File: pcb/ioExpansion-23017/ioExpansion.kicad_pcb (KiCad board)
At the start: 2 copper layers, 16 parts, among them J1 GS3, J2 GS3, J3 GS3, U1 MCP23017, U2 Header2

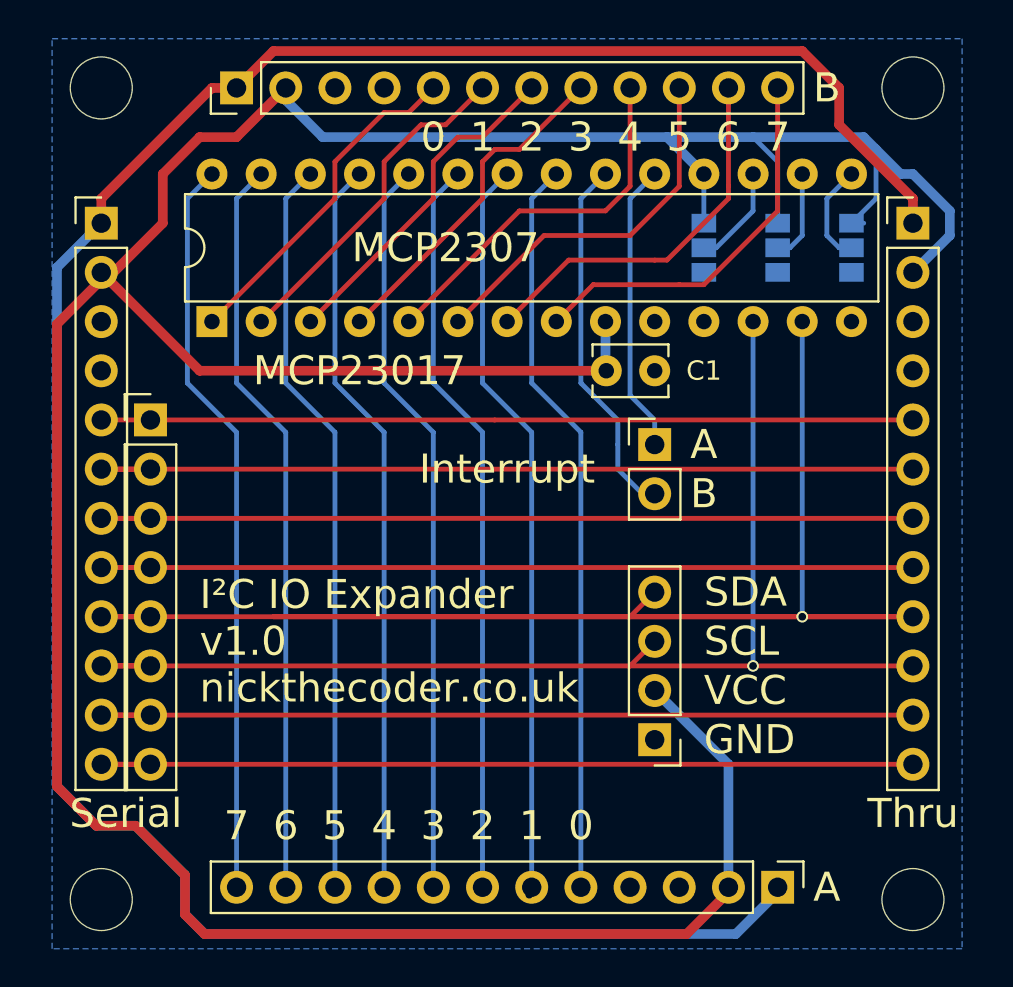
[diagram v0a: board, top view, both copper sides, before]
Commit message: Added extra I2C headers to the ioExpansion module.
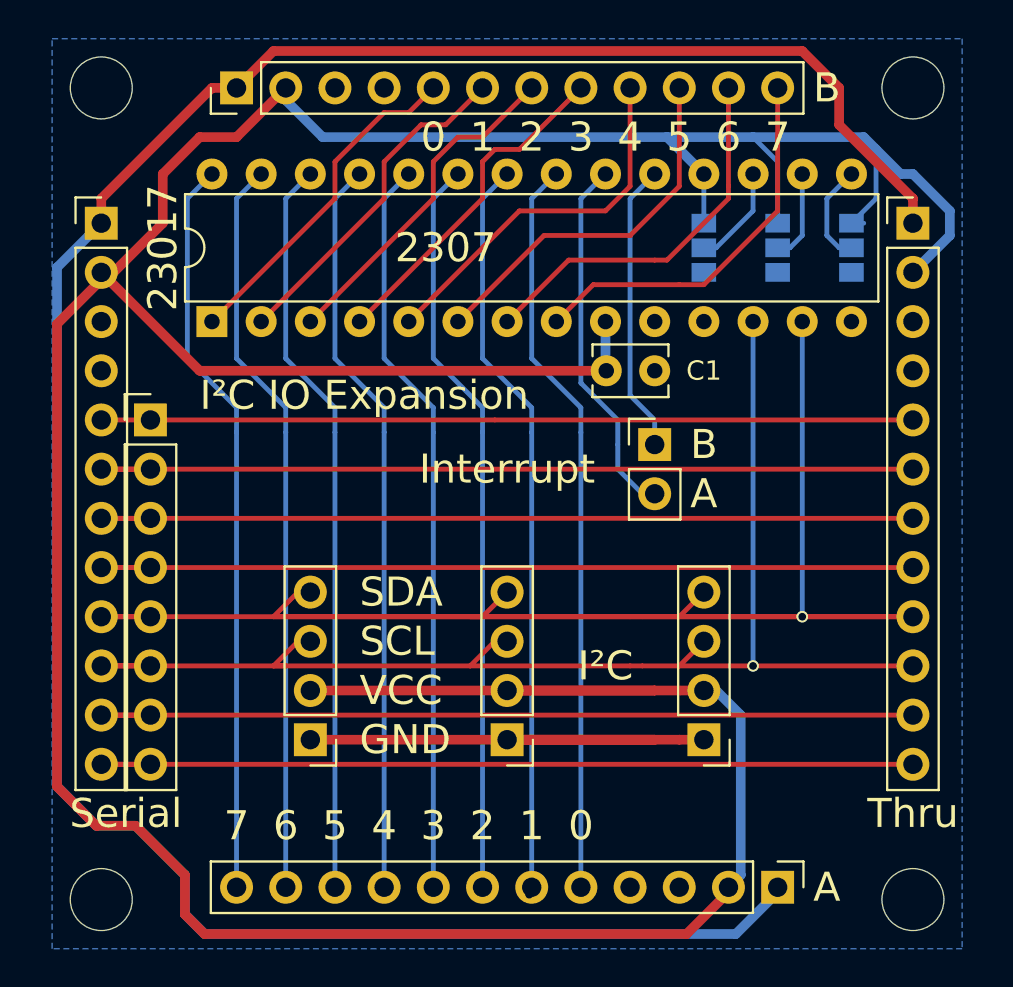
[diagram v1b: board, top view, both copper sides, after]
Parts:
- removed U2: Header2, Pin_Headers:Pin_Header_Straight_1x02_Pitch2.54mm
- added I2C2: I2CHeader, Pin_Headers:Pin_Header_Straight_1x04_Pitch2.54mm, F.Cu at (139.1, 120.0)
- added I2C3: I2CHeader, Pin_Headers:Pin_Header_Straight_1x04_Pitch2.54mm, F.Cu at (149.2, 120.0)
- added J4: Interrupt, Pin_Headers:Pin_Header_Straight_1x02_Pitch2.54mm, F.Cu at (156.8, 104.8)
- moved I2C1 2.54 mm to (159.4, 120.0)
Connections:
- U1 pad 19: /IA -> /IB
- U1 pad 20: /IB -> /IA
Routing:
- net /GND: track 0.00 -> 27.9 mm
- net /VCC: track 181.1 -> 208.9 mm
- net /L5: track 64.0 -> 69.5 mm
- net /L4: track 95.1 -> 100.0 mm
- net /IB: track 19.0 -> 15.0 mm
- net /IA: track 15.0 -> 19.0 mm
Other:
- board text added: "23017"
- board text added: "2307"
- board text added: "I²C"
- board text added: "I²C IO Expansion"
- board text added: "I²C IO Expansion v1.0 nickthecoder.co.uk"
- board text removed: "I²C IO Expander v1.0 nickthecoder.co.uk"
- board text removed: "MCP23017"
- board text removed: "MCP2307"
